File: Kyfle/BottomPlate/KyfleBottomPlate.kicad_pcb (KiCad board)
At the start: 2 copper layers, 160.8 x 138.4 mm, 50 parts, among them SW2 KEY_SWITCH, SW2 PRO MICRO

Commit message: Adding 3D model for cherry mx (from Acheron libs), adding generating pretty pictures with it
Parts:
- removed the SW2 at (188.1, 98.5)
- added SW2: KEY_SWITCH, SofleChocTop:SU120_RGB_SW_Bottom_No_Rail_no_silk, F.Cu at (103.9, 142.1)
- added SW2: KEY_SWITCH, SofleChocTop:SU120_RGB_SW_Bottom_No_Rail_no_silk, F.Cu at (151.1, 118.8)
- added SW2: KEY_SWITCH, SofleChocTop:SU120_RGB_SW_Bottom_No_Rail_no_mx, F.Cu at (188.1, 98.5)
- added SW2: KEY_SWITCH, SofleChocTop:SU120_RGB_SW_Bottom_No_Rail_no_silk, F.Cu at (130.9, 111.1)
- added SW2: KEY_SWITCH, SofleChocTop:SU120_RGB_SW_Bottom_No_Rail_no_silk, F.Cu at (130.9, 92.0)
- added SW2: KEY_SWITCH, SofleChocTop:SU120_RGB_SW_Bottom_No_Rail_no_silk, F.Cu at (130.9, 73.0)
- added SW2: KEY_SWITCH, SofleChocTop:SU120_RGB_SW_Bottom_No_Rail_no_mx, F.Cu at (130.9, 44.4)
- SW2 (x2): footprint SofleChocTop:SU120_RGB_SW_2u_Bottom -> SofleChocTop:SU120_RGB_SW_2u_Bottom_no_mx
- SW2 (x13): footprint SofleChocTop:SU120_RGB_SW_Bottom_No_Rail -> SofleChocTop:SU120_RGB_SW_Bottom_No_Rail_no_mx
- SW2 (x12): footprint SofleChocTop:SU120_RGB_SW_Bottom -> SofleChocTop:SU120_RGB_SW_Bottom_no_mx
- SW2: footprint SofleChocTop:SU120_RGB_SW_Bottom_No_Rail -> SofleChocTop:SU120_RGB_SW_Bottom_No_Rail_no_silk
- moved SW2 9.53 mm to (130.9, 53.9)

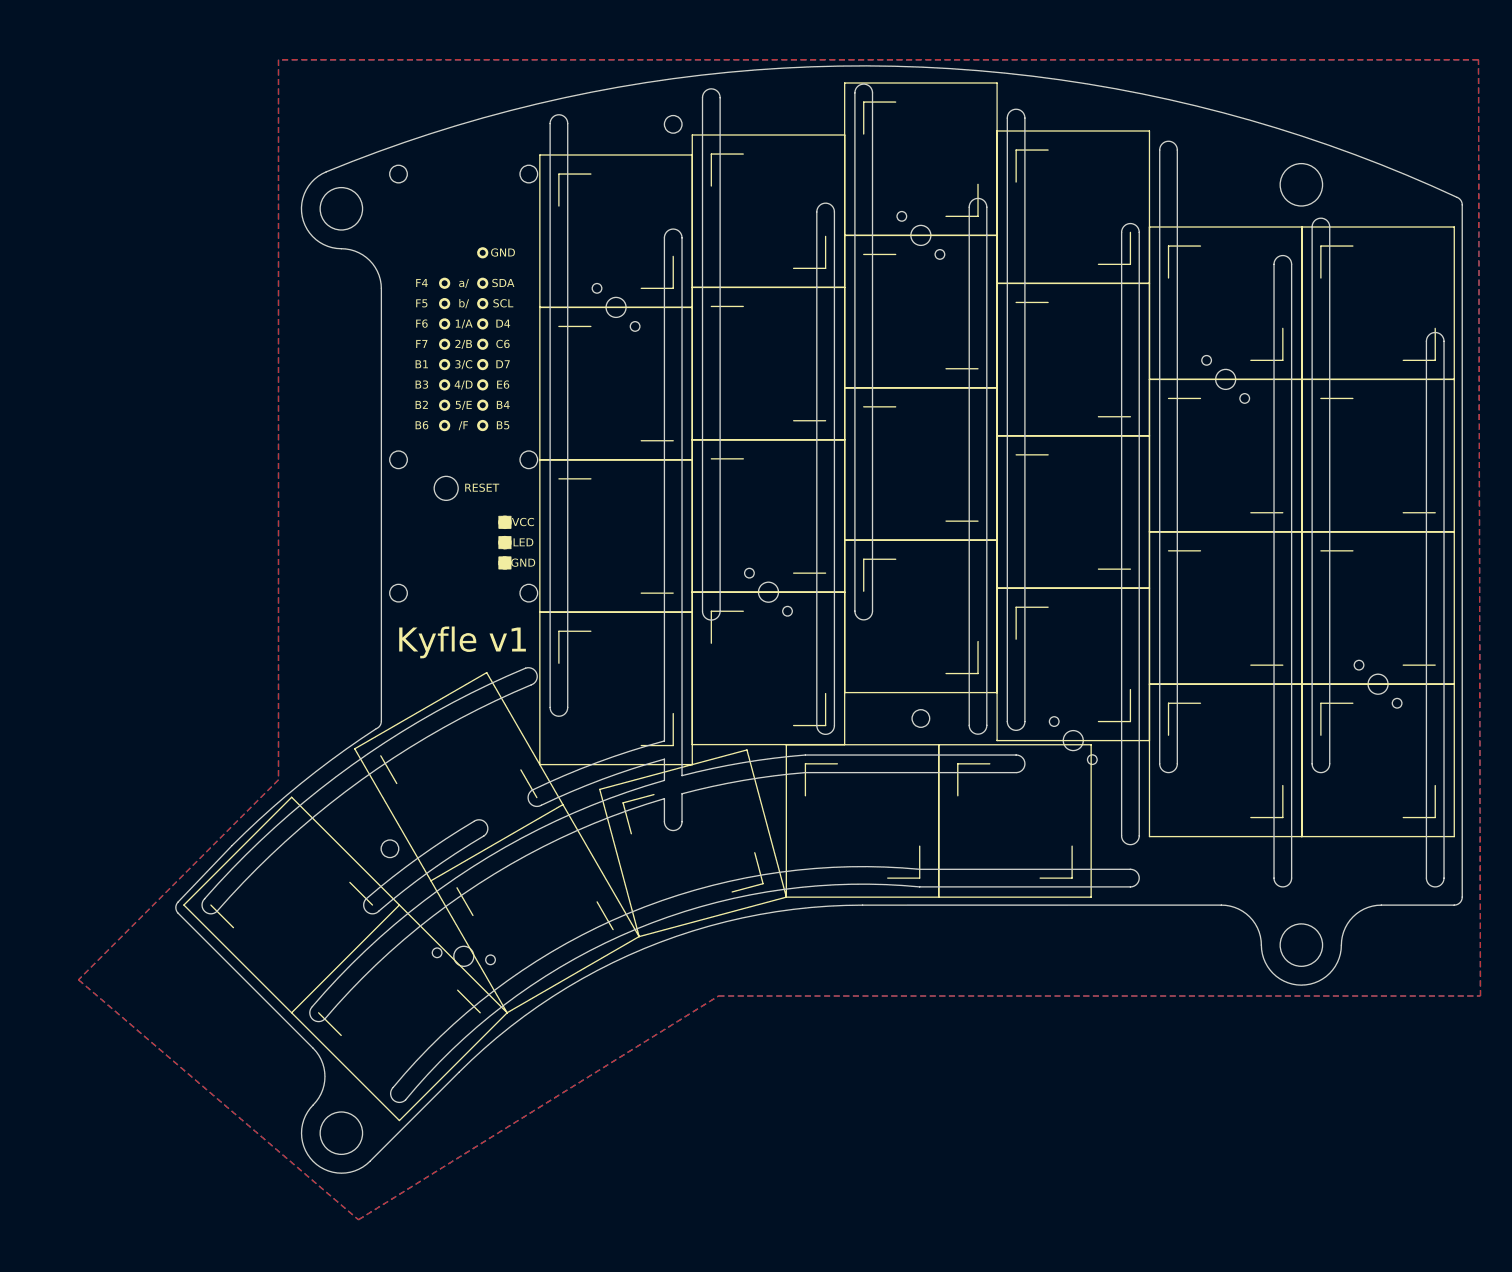
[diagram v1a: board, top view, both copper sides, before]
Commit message: Adding reference positions to bottom plate silk screen
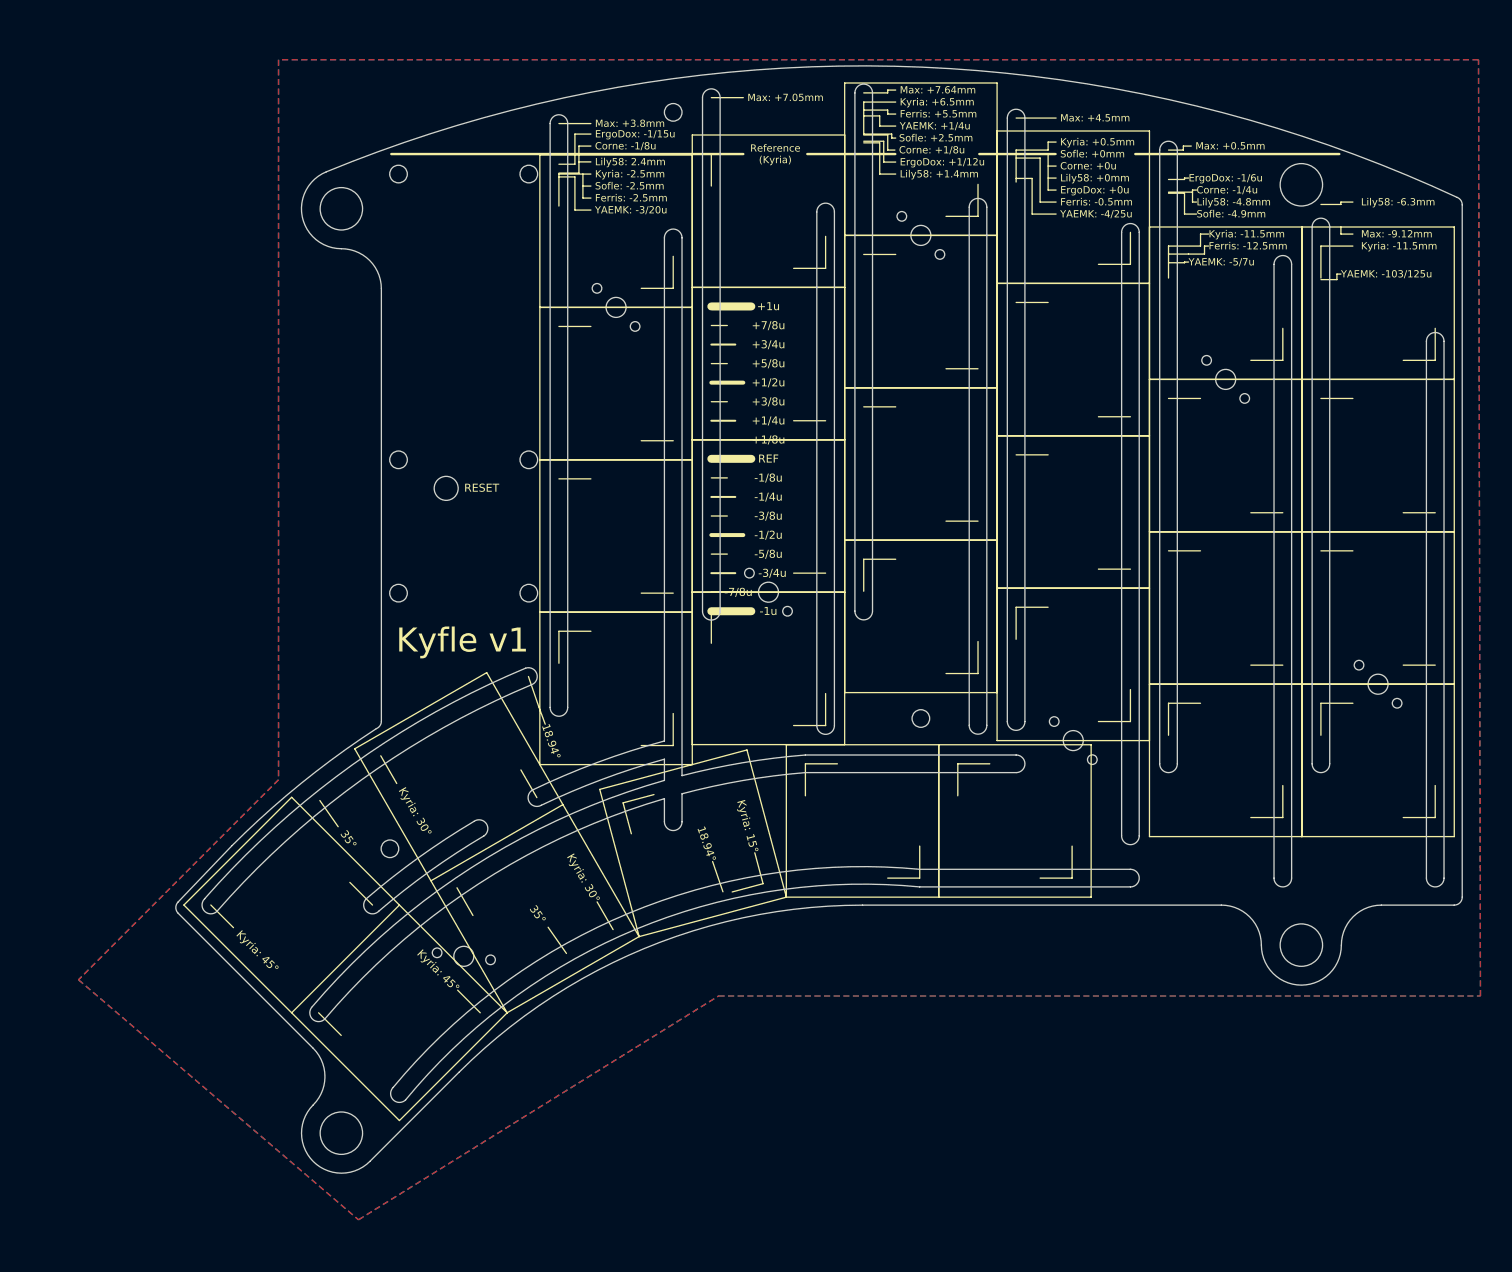
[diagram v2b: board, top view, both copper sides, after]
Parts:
- removed the SW2 at (130.9, 111.1)
- removed the SW2 at (130.9, 92.0)
- removed the SW2 at (130.9, 73.0)
- removed the SW2 at (130.9, 53.9)
- SW2 (x2): footprint SofleChocTop:SU120_RGB_SW_2u_Bottom_no_mx -> SofleChocTop:SU120_RGB_SW_2u_Bottom
- SW2 (x12): footprint SofleChocTop:SU120_RGB_SW_Bottom_no_mx -> SofleChocTop:SU120_RGB_SW_Bottom
- SW2 (x15): footprint SofleChocTop:SU120_RGB_SW_Bottom_No_Rail_no_mx -> SofleChocTop:SU120_RGB_SW_Bottom_No_Rail
- moved TH3 1.50 mm to (138.1, 29.5)
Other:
- board text added: "+1/2u"
- board text added: "+1/4u"
- board text added: "+1/8u"
- board text added: "+1u"
- board text added: "+3/4u"
- board text added: "+3/8u"
- board text added: "+5/8u"
- board text added: "+7/8u"
- board text added: "-1/2u"
- board text added: "-1/4u"
- board text added: "-1/8u"
- board text added: "-1u"
- board text added: "-3/4u"
- board text added: "-3/8u"
- board text added: "-5/8u"
- board text added: "-7/8u"
- board text added: "Corne: +0u"
- board text added: "Corne: +1/8u"
- board text added: "Corne: -1/4u"
- board text added: "Corne: -1/8u"
- board text added: "ErgoDox: +0u"
- board text added: "ErgoDox: +1/12u"
- board text added: "ErgoDox: -1/15u"
- board text added: "ErgoDox: -1/6u"
- board text added: "Ferris: +5.5mm"
- board text added: "Ferris: -0.5mm"
- board text added: "Ferris: -12.5mm"
- board text added: "Ferris: -2.5mm"
- board text added: "Kyria: +0.5mm"
- board text added: "Kyria: +6.5mm"
- board text added: "Kyria: -11.5mm"
- board text added: "Kyria: -2.5mm"
- board text added: "Kyria: 15°"
- board text added: "Kyria: 30°"
- board text added: "Kyria: 45°"
- board text added: "Lily58: +0mm"
- board text added: "Lily58: +1.4mm"
- board text added: "Lily58: -4.8mm"
- board text added: "Lily58: -6.3mm"
- board text added: "Lily58: 2.4mm"
- board text added: "Max: +0.5mm"
- board text added: "Max: +3.8mm"
- board text added: "Max: +4.5mm"
- board text added: "Max: +7.05mm"
- board text added: "Max: +7.64mm"
- board text added: "Max: -9.12mm"
- board text added: "REF"
- board text added: "Reference (Kyria)"
- board text added: "Sofle: +0mm"
- board text added: "Sofle: +2.5mm"
- board text added: "Sofle: -2.5mm"
- board text added: "Sofle: -4.9mm"
- board text added: "YAEMK: +1/4u"
- board text added: "YAEMK: -103/125u"
- board text added: "YAEMK: -3/20u"
- board text added: "YAEMK: -4/25u"
- board text added: "YAEMK: -5/7u"

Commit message: Massive redesign
- Realised the design was not reversible. Only solution was to mirror the two diagonal holes of each bit. But one of them was coliding with hotswap socket footprint. Until...
- I also realised that having the holes at these Y positions made the screw coming on top collide with the bottom of the switch housing...
- So switched to having two holes right in between each bit (vertically).
- Then I realised cheap pcb houses can have quite some limitations when it comes to exotic uses of slots. In particular, for jlcpcb:
  * They prefer tabs to be >= 4mm wide
  * They prefer at least 3mm of PCB next to a slot (ie. avoid slim inter-slots parts)
  * They prefer 0.4mm clearence from board edge when it is milled/routed
  * Watching some videos of their fab it seems they do the edge.cuts routing with a single 1mm bit. Ie. if you specify a larger radius they actually route it out. And if you specify a smaller radius (than 0.5mm) they cannot do it.

So, I redid the PCB. Twice... Again. For now...

I also started reorganising the projects. First part was to gather all footprints used accross the three boards. Makes cross-board editing of footprints easier.
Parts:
- removed the SW2 at (103.9, 142.1)
- removed the SW2 at (151.1, 118.8)
- added SW2: KEY_SWITCH, Kyfle Footprints:CherryMX_Kyfle_v1_BottomPlate_2u, F.Cu at (132.0, 113.6)
- REF** (x4): footprint SofleChocTop:M5_with_washer -> Kyfle Footprints:M5_with_washer
- REF** (x6), TH3, TH7 (x2): footprint SofleChocTop:M2_with_washer -> Kyfle Footprints:M2_with_washer
- SW2 (x15): footprint SofleChocTop:SU120_RGB_SW_Bottom_No_Rail -> Kyfle Footprints:CherryMX_Kyfle_v1_BottomPlate_1u_No_Rail
- SW2 (x12): footprint SofleChocTop:SU120_RGB_SW_Bottom -> Kyfle Footprints:CherryMX_Kyfle_v1_BottomPlate_1u
- SW2 (x2): footprint SofleChocTop:SU120_RGB_SW_2u_Bottom -> Kyfle Footprints:CherryMX_Kyfle_v1_BottomPlate_2u
- SW2: footprint SofleChocTop:SU120_ProMicro_Bottom -> Kyfle Footprints:Arduino_ProMicro_Kyfle_v1_BottomPlate
- SW2 (x7): footprint SofleChocTop:SK6812_Bit_Bottom -> Kyfle Footprints:SK6812_Bit_Bottom

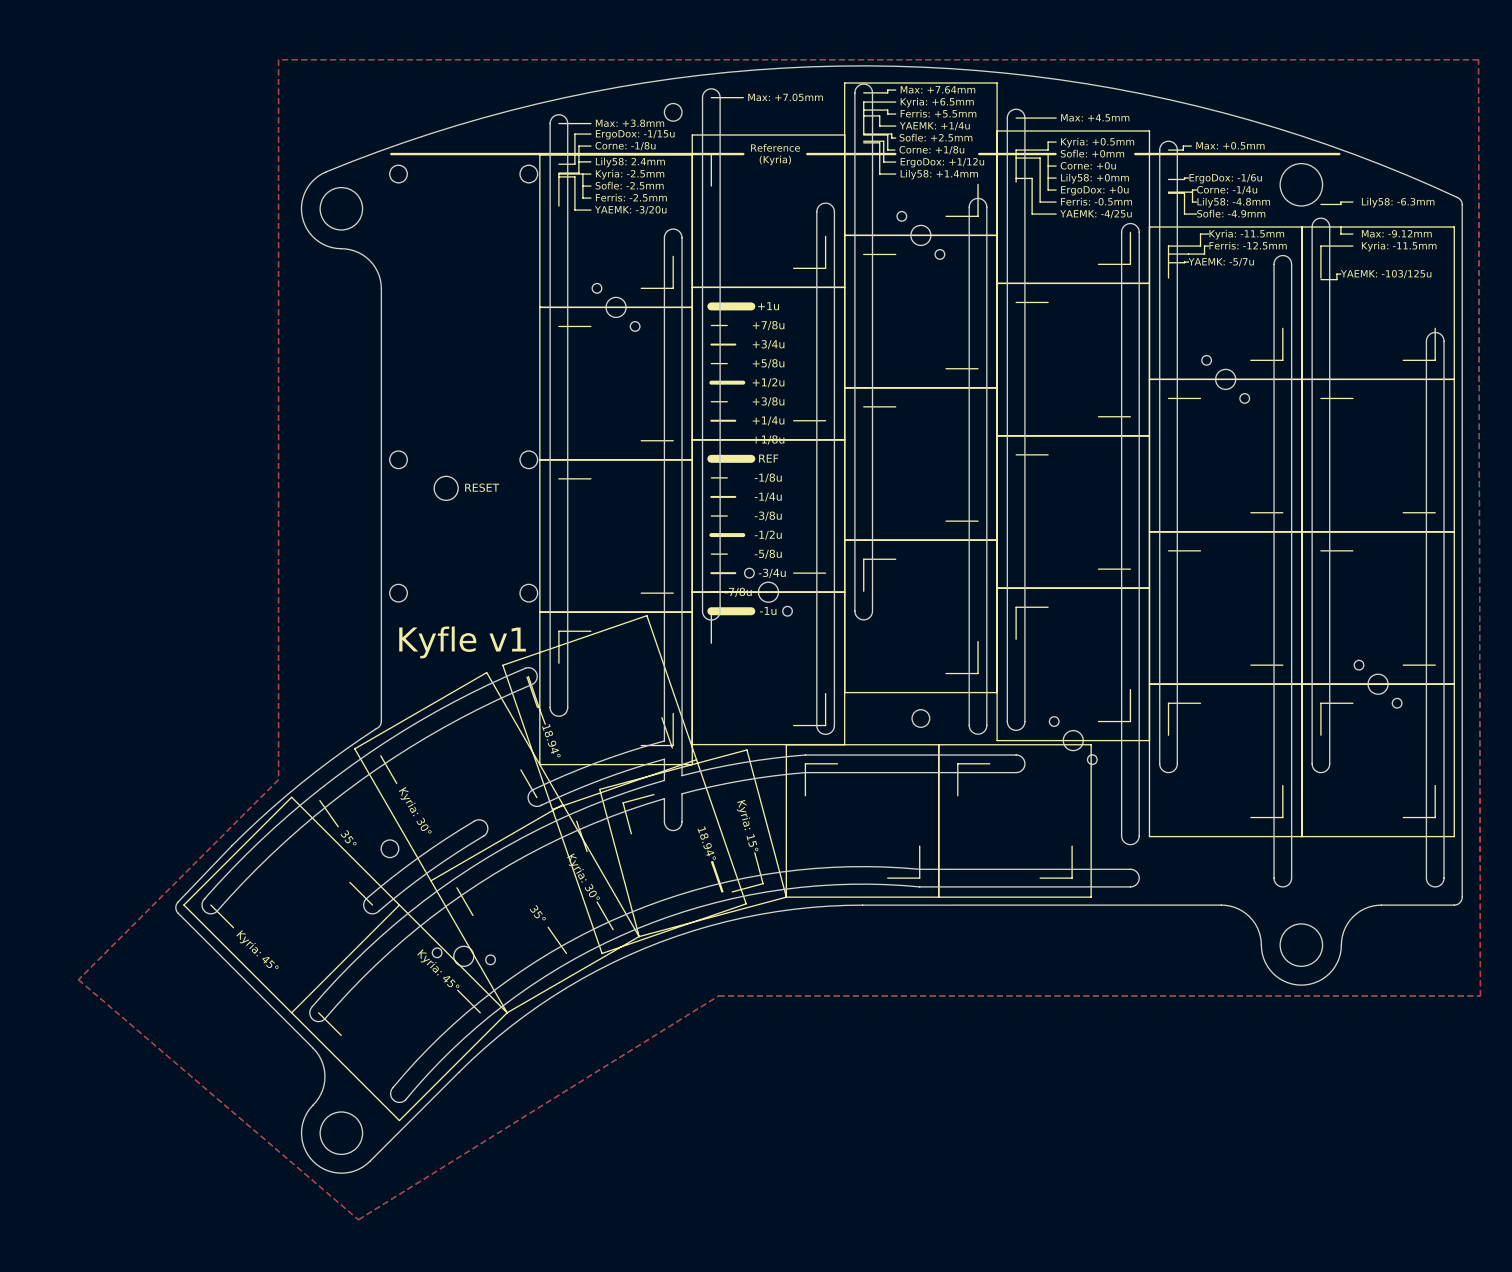
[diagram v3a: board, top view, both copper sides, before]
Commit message: PCB done. Started redoing the rails.
- PCB should be in its final version now, pretty much. I hope...
- I added a tentative compatibility with Panasonic roller encoders.
- Also added some silk screens for the 2u stabilisers.
- Propagated the new bit board design to footprints used for top and bottom plate.
- And started to rework the rails in the bottom plate, as well as the general shape of the keyboard.
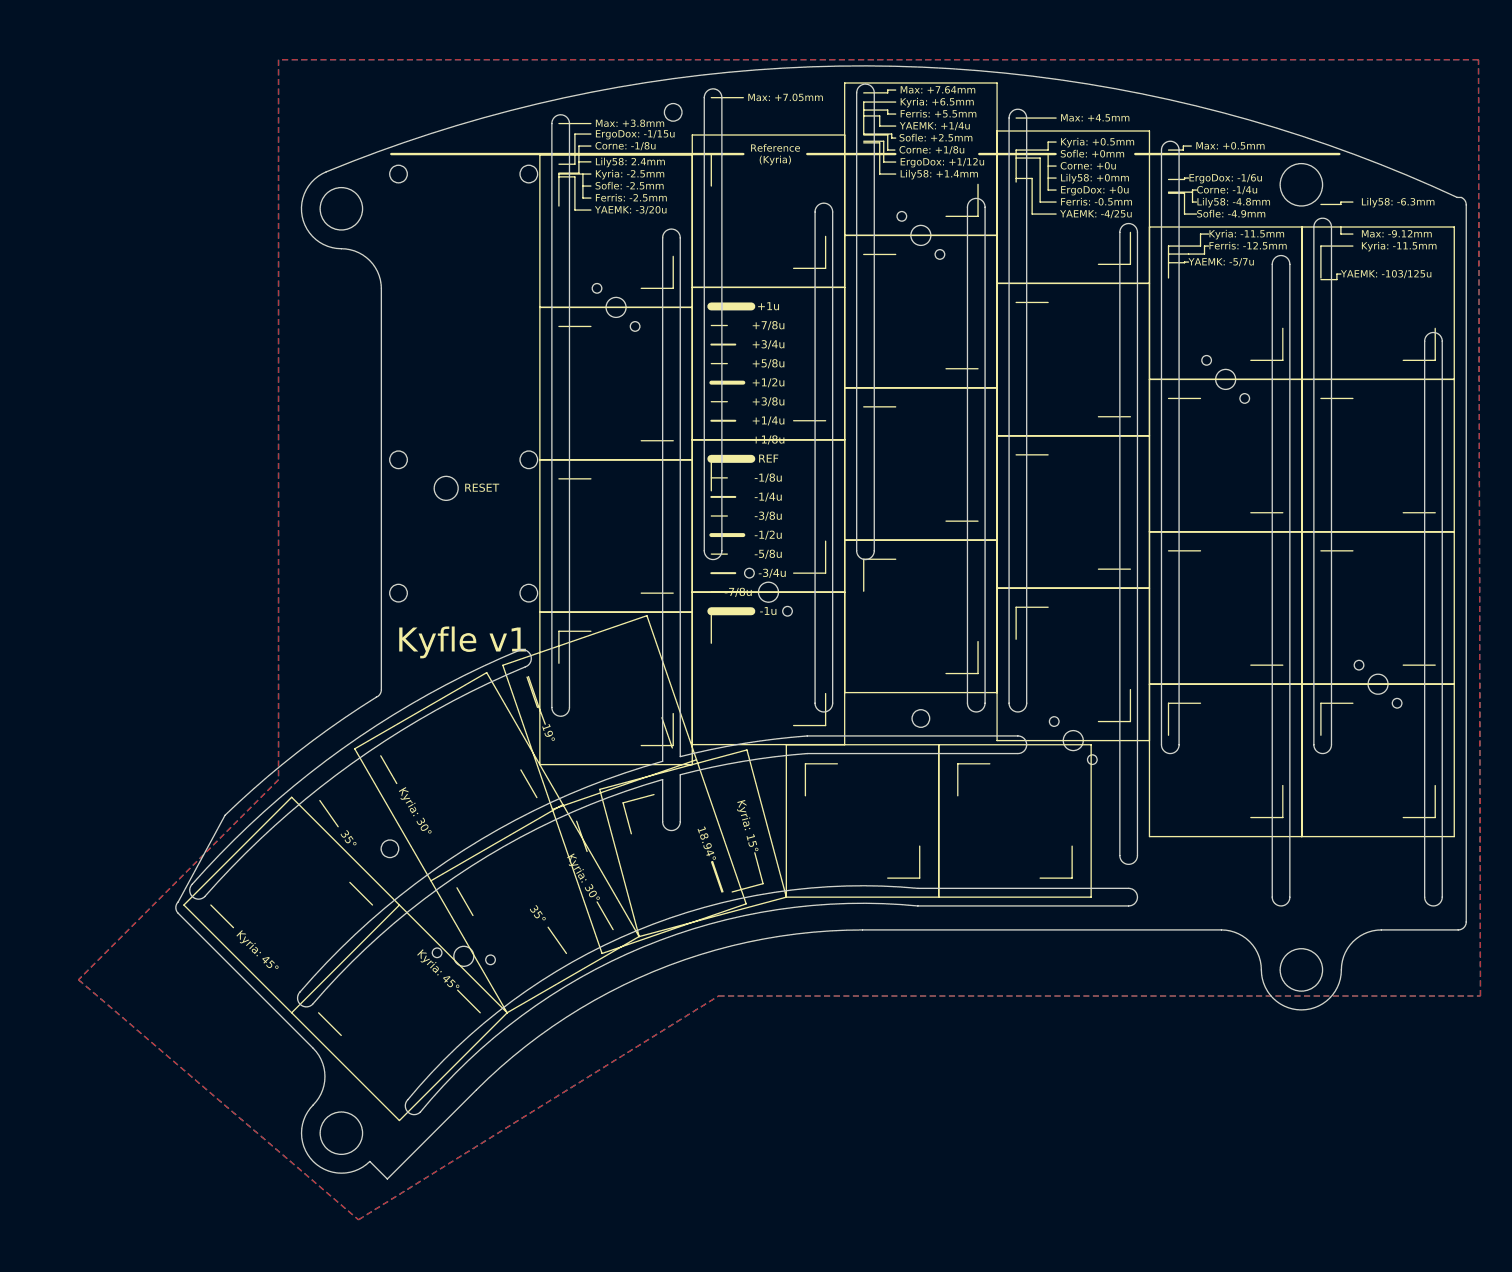
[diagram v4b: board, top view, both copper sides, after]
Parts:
- added Spacer: KEY_SWITCH, Kyfle Footprints:CherryMX_Kyfle_v1_BottomPlate_1u_Mount_Spacing, F.Cu at (124.0, 103.9)
- SW2: footprint Kyfle Footprints:CherryMX_Kyfle_v1_BottomPlate_1u -> Kyfle Footprints:CherryMX_Kyfle_v1_BottomPlate_1u_No_Rail
- moved REF** 3.10 mm to (216.6, 136.7)
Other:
- board size 160.8 x 138.4 mm -> 161.3 x 139.1 mm
- board text added: "19°"
